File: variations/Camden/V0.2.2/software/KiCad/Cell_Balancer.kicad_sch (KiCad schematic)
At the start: 12 parts, among them J1 Screw_Terminal_01x11, J2 DC37_Pins

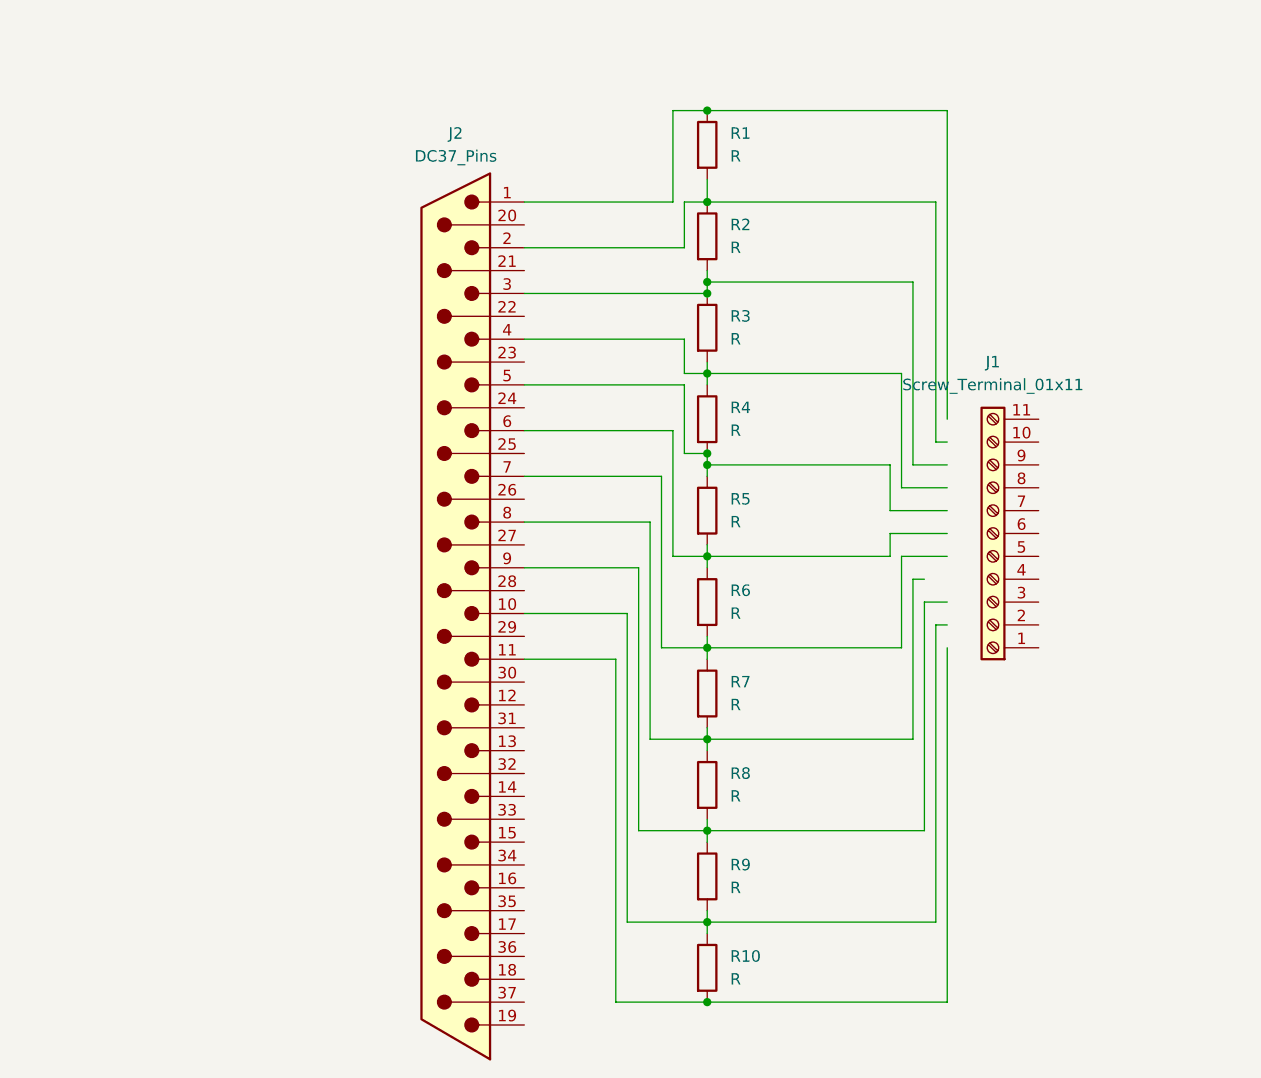
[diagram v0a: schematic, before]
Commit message: KiCAD update
figured out the issue with the pcb copper tracks, software crashed a couple of times so there are a lot of autosaves, next step is getting the mounting holes the right size and correct distance then it will be ready to go
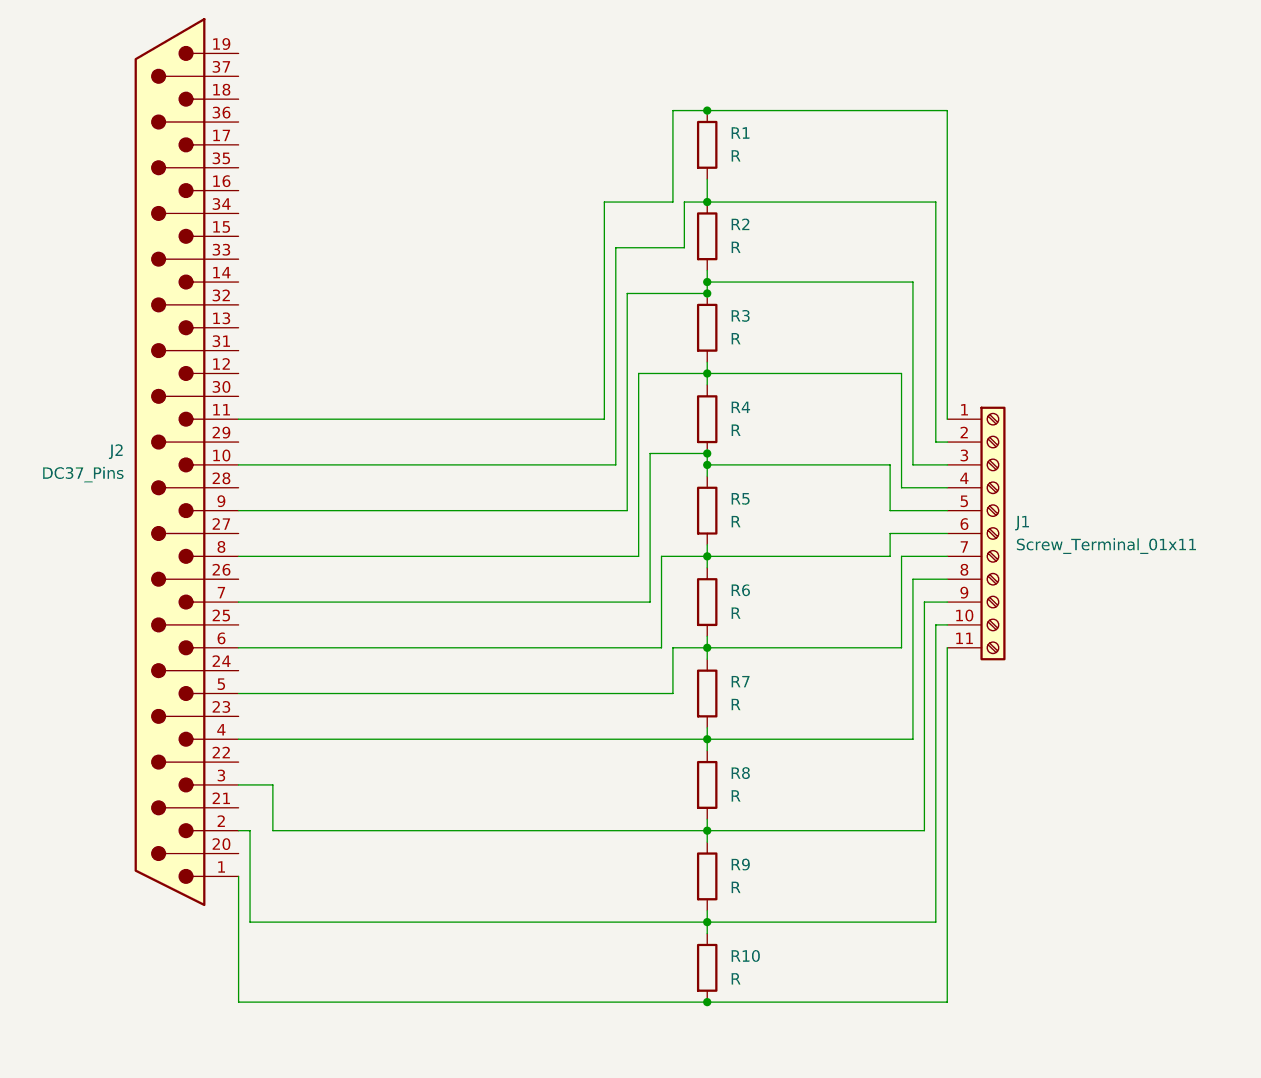
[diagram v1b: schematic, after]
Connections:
- net at R1.1: now also J1.1 (Pin_1), J2.11; no longer J2.1
- net at R1.2, R2.1: now also J1.2 (Pin_2), J2.10; no longer J2.2
- net at R2.2, R3.1: now also J1.3 (Pin_3), J2.9; no longer J2.3
- net at R7.2, R8.1: now also J1.8 (Pin_8), J2.4; no longer J2.8
- net at R8.2, R9.1: now also J1.9 (Pin_9), J2.3; no longer J2.9
- net at J1.10 (Pin_10): now also J2.2, R10.1, R9.2
- net at J1.11 (Pin_11): now also J2.1, R10.2
- net at J1.4 (Pin_4): now also J2.8, R3.2, R4.1
- net at J1.5 (Pin_5): now also J2.7, R4.2, R5.1
- net at J1.6 (Pin_6): now also J2.6, R5.2, R6.1
- net at J1.7 (Pin_7): now also J2.5, R6.2, R7.1
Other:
- moved on the sheet: J1

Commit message: update
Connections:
- net at J1.1 (Pin_1), R1.1: now also J2.13; no longer J2.11
- net at J1.2 (Pin_2), R1.2, R2.1: now also J2.12; no longer J2.10
- net at J1.3 (Pin_3), R2.2, R3.1: now also J2.11; no longer J2.9
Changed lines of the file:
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@@
-	(wire
-		(pts
-			(xy 101.6 69.85) (xy 60.96 69.85)
-		)
-		(stroke
-			(width 0)
-			(type default)
-		)
-	)
 	(wire
 		(pts
@@
 	(wire
 		(pts
+			(xy 60.96 64.77) (xy 102.87 64.77)
+		)
+		(stroke
+			(width 0)
+			(type default)
+		)
+	)
+	(wire
+		(pts
 			(xy 113.03 124.46) (xy 113.03 125.73)
 		)
@@
 	(wire
 		(pts
+			(xy 101.6 45.72) (xy 101.6 59.69)
+		)
+		(stroke
+			(width 0)
+			(type default)
+		)
+	)
+	(wire
+		(pts
 			(xy 113.03 83.82) (xy 113.03 85.09)
 		)
@@
 	(wire
 		(pts
-			(xy 104.14 55.88) (xy 104.14 80.01)
-		)
-		(stroke
-			(width 0)
-			(type default)
-		)
-	)
-	(wire
-		(pts
 			(xy 113.03 125.73) (xy 113.03 127)
 		)
@@
 	(wire
 		(pts
-			(xy 101.6 45.72) (xy 101.6 69.85)
+			(xy 102.87 50.8) (xy 102.87 64.77)
 		)
 		(stroke
@@
 	(wire
 		(pts
-			(xy 102.87 50.8) (xy 102.87 74.93)
-		)
-		(stroke
-			(width 0)
-			(type default)
-		)
-	)
-	(wire
-		(pts
 			(xy 135.89 87.63) (xy 135.89 105.41)
 		)
@@
 	(wire
 		(pts
+			(xy 60.96 69.85) (xy 104.14 69.85)
+		)
+		(stroke
+			(width 0)
+			(type default)
+		)
+	)
+	(wire
+		(pts
 			(xy 113.03 85.09) (xy 113.03 86.36)
 		)
@@
 	(wire
 		(pts
+			(xy 60.96 59.69) (xy 101.6 59.69)
+		)
+		(stroke
+			(width 0)
+			(type default)
+		)
+	)
+	(wire
+		(pts
 			(xy 134.62 85.09) (xy 134.62 95.25)
 		)
@@
 	(wire
 		(pts
-			(xy 102.87 74.93) (xy 60.96 74.93)
-		)
-		(stroke
-			(width 0)
-			(type default)
-		)
-	)
-	(wire
-		(pts
 			(xy 113.03 74.93) (xy 113.03 76.2)
 		)
@@
 	(wire
 		(pts
-			(xy 104.14 80.01) (xy 60.96 80.01)
-		)
-		(stroke
-			(width 0)
-			(type default)
-		)
-	)
-	(wire
-		(pts
 			(xy 135.89 54.61) (xy 113.03 54.61)
 		)
@@
 		)
 		(stroke
+			(width 0)
+			(type default)
+		)
+	)
+	(wire
+		(pts
+			(xy 104.14 55.88) (xy 104.14 69.85)
+		)
+		(stroke
